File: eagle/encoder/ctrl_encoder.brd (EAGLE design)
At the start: 25.5 x 25.5 mm, 14 parts, among them J1 PAD+SQUARE-1.5X1.5, J10 PAD+SQUARE-1.5X1.5, J11 PAD+SQUARE-1.5X1.5, J2 PAD+SQUARE-1.5X1.5, J3 PAD+SQUARE-1.5X1.5, J4 PAD+SQUARE-1.5X1.5, J5 PAD+SQUARE-1.5X1.5, J6 PAD+SQUARE-1.5X1.5, J7 PAD+SQUARE-1.5X1.5, J9 PAD+SQUARE-1.5X1.5

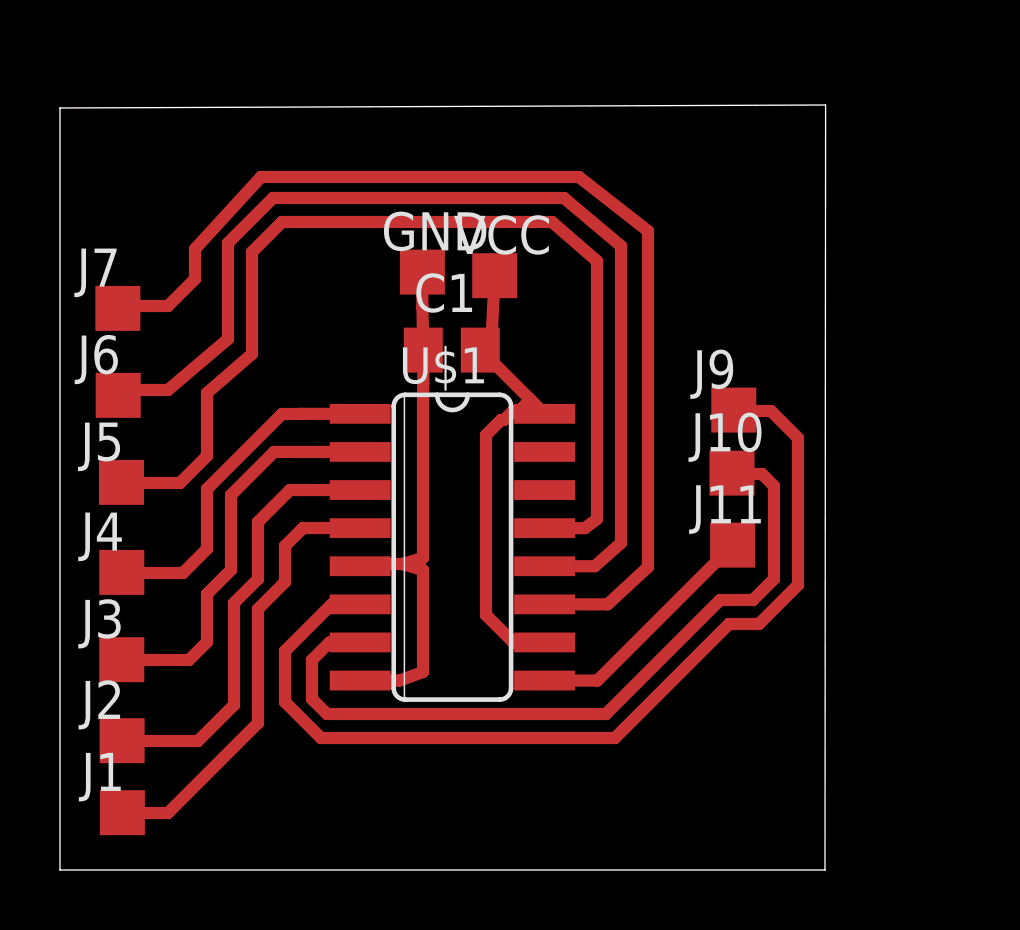
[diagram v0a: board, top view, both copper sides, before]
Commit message: moved j1-j8 pins up on the ctrl_encoder.brd shrinking the actual size of the encoder board by several mm.
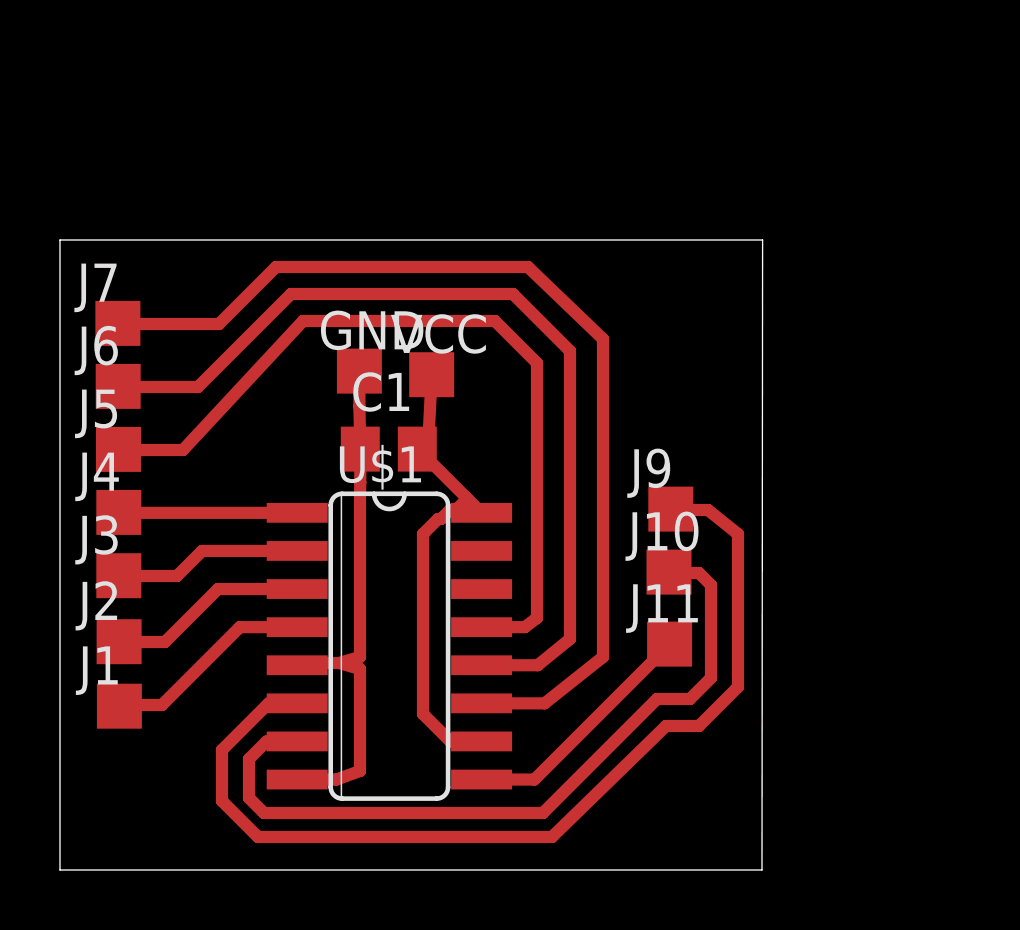
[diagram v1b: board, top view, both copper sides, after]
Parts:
- moved J9 3.91 mm to (20.4, 12.0)
- moved J11 3.91 mm to (20.3, 7.53)
- moved GND 3.91 mm to (9.98, 16.6)
- moved J10 3.91 mm to (20.3, 9.93)
- moved U$1 3.91 mm to (11.0, 7.46)
- moved C1 3.91 mm to (11.0, 14.0)
- moved VCC 3.91 mm to (12.4, 16.5)
- moved J1 3.55 mm to (1.98, 5.46)
- moved J2 3.30 mm to (1.97, 7.61)
- moved J3 2.80 mm to (1.96, 9.81)
- moved J4 2.00 mm to (1.96, 11.9)
- moved J5 1.10 mm to (1.95, 14.0)
- moved J7 0.50 mm to (1.93, 18.2)
- moved J6 0.30 mm to (1.94, 16.1)
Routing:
- net N$4: track 14.5 -> 6.67 mm
- net N$3: track 14.8 -> 7.02 mm
- net N$5: track 13.2 -> 6.30 mm
- net N$7: track 33.6 -> 26.9 mm
- net N$6: track 11.3 -> 5.96 mm
- net N$8: track 34.6 -> 30.0 mm
- net N$9: track 35.9 -> 33.1 mm
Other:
- board size 25.5 x 25.5 mm -> 23.4 x 21 mm

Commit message: Replaced surface mount pads with through hole pads.  Added a polygon to the .brd and increased the size of the isolate from 10mil to 20mils, this should prevent solder from bridging to the remaining copper on the test board.  Also increased the spacing of the pads.
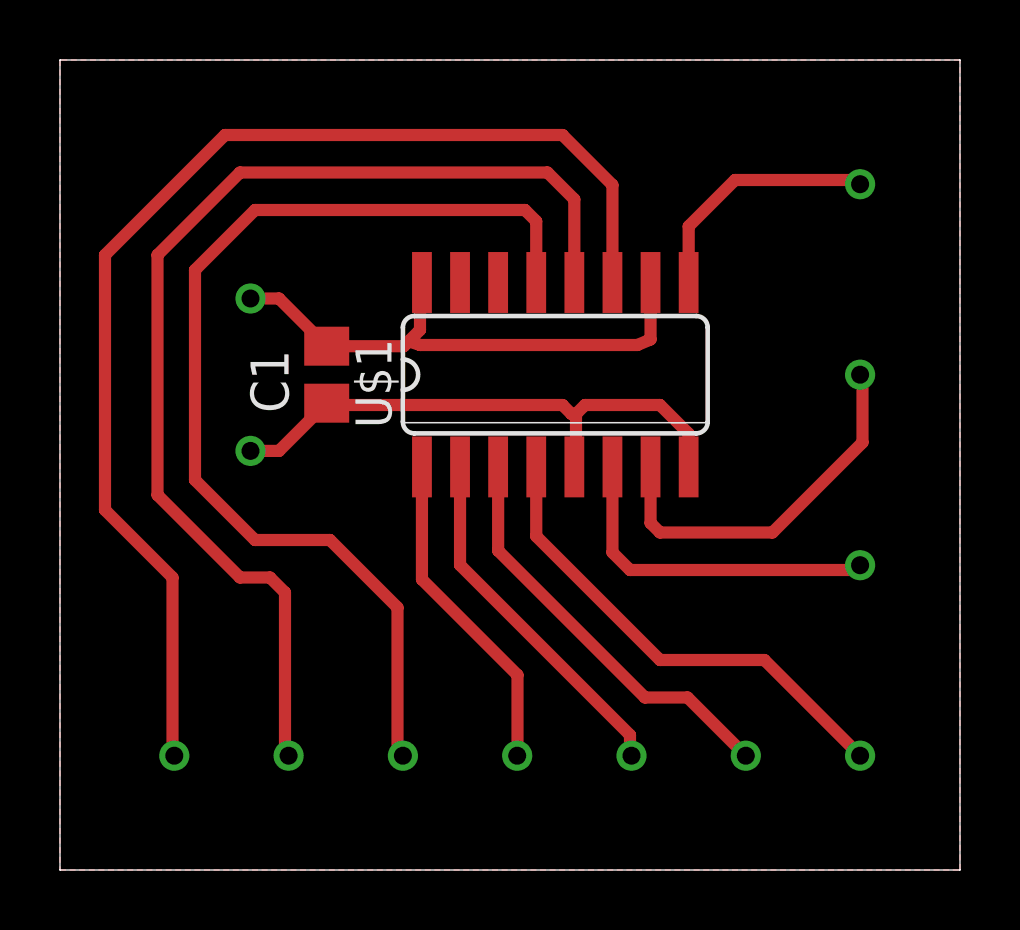
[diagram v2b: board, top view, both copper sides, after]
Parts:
- GND, J1, J10, J11, J2, J3, J4, J5, J6, J7, J9, VCC: value PAD+SQUARE-1.5X1.5 -> PAD; device LockBox:PAD-1.5X1.5 -> LockBox:TEST_PAD
- moved J1 24.7 mm to (26.7, 3.81), turned to 90 degrees
- moved J2 21.2 mm to (22.9, 3.81), turned to 90 degrees
- moved J3 18.1 mm to (19.1, 3.81), turned to 90 degrees
- moved J11 16.6 mm to (26.7, 22.9), turned to 90 degrees
- moved J4 15.6 mm to (15.2, 3.81), turned to 90 degrees
- moved J7 14.5 mm to (3.81, 3.81), turned to 90 degrees
- moved J5 13.9 mm to (11.4, 3.81), turned to 90 degrees
- moved J6 13.6 mm to (7.62, 3.81), turned to 90 degrees
- moved U$1 10.6 mm to (16.5, 16.5), turned to 0 degrees
- moved J10 9.16 mm to (26.7, 16.5), turned to 90 degrees
- moved J9 6.58 mm to (26.7, 10.2), turned to 90 degrees
- moved VCC 6.55 mm to (6.35, 19.1), turned to 90 degrees
- moved GND 4.50 mm to (6.35, 14.0), turned to 90 degrees
- moved C1 3.23 mm to (8.89, 16.5), turned to 90 degrees
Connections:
- net GND: now also GND.P$1; no longer GND.PAD
- net N$1: now also VCC.P$1; no longer VCC.PAD
- net N$11: now also J10.P$1; no longer J10.PAD
- net N$12: now also J11.P$1; no longer J11.PAD
- net N$2: now also J9.P$1; no longer J9.PAD
- net N$3: now also J1.P$1; no longer J1.PAD
- net N$4: now also J2.P$1; no longer J2.PAD
- net N$5: now also J3.P$1; no longer J3.PAD
- net N$6: now also J4.P$1; no longer J4.PAD
- net N$7: now also J5.P$1; no longer J5.PAD
- net N$8: now also J6.P$1; no longer J6.PAD
- net N$9: now also J7.P$1; no longer J7.PAD
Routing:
- net N$2: track 32.2 -> 11.4 mm
- net N$11: track 25.3 -> 12.6 mm
- net N$3: track 7.02 -> 16.1 mm
- net N$7: track 26.9 -> 34.9 mm
- net N$8: track 30.0 -> 37.3 mm
- net N$4: track 6.67 -> 13.9 mm
- net N$9: track 33.1 -> 40.2 mm
- net N$5: track 6.30 -> 12.0 mm
- net N$6: track 5.96 -> 11.0 mm
- net N$1: track 15.9 -> 18.2 mm
- net GND: track 18.0 -> 18.8 mm
- added copper zone on layer 1, net N$10
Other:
- board size 23.4 x 21 mm -> 30 x 27 mm
